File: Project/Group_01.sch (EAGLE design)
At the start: 1 part

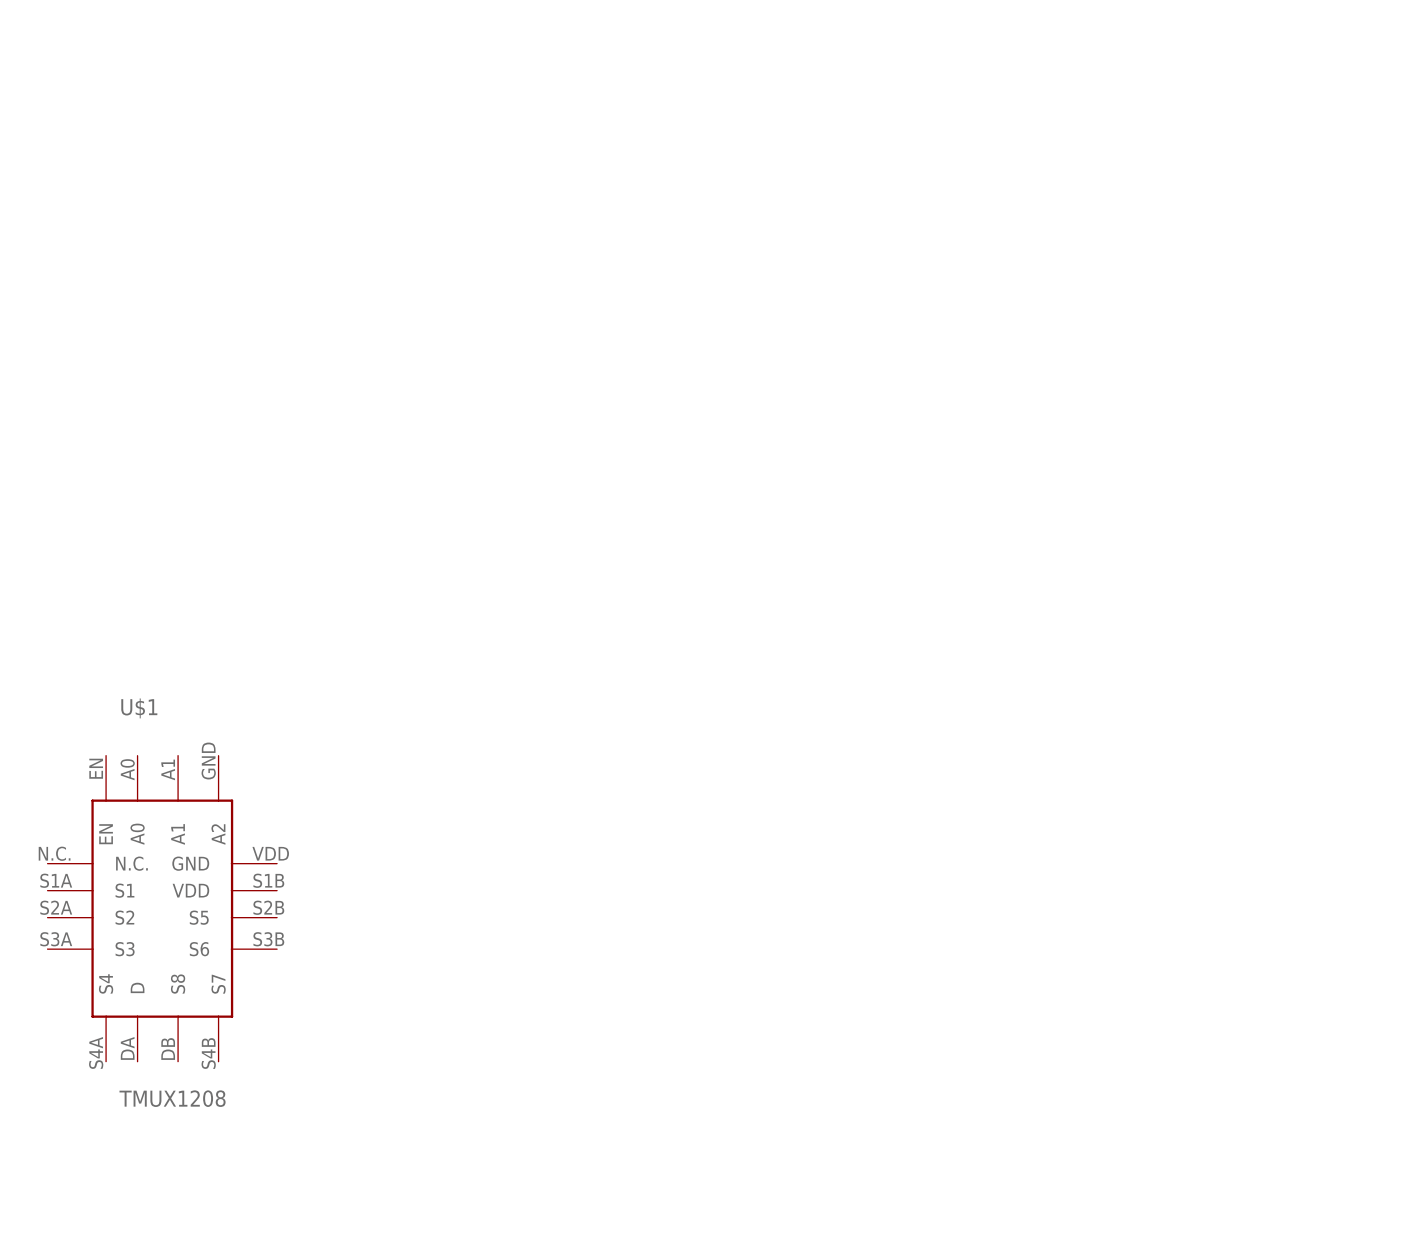
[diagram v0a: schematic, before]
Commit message: Added all components to schematics
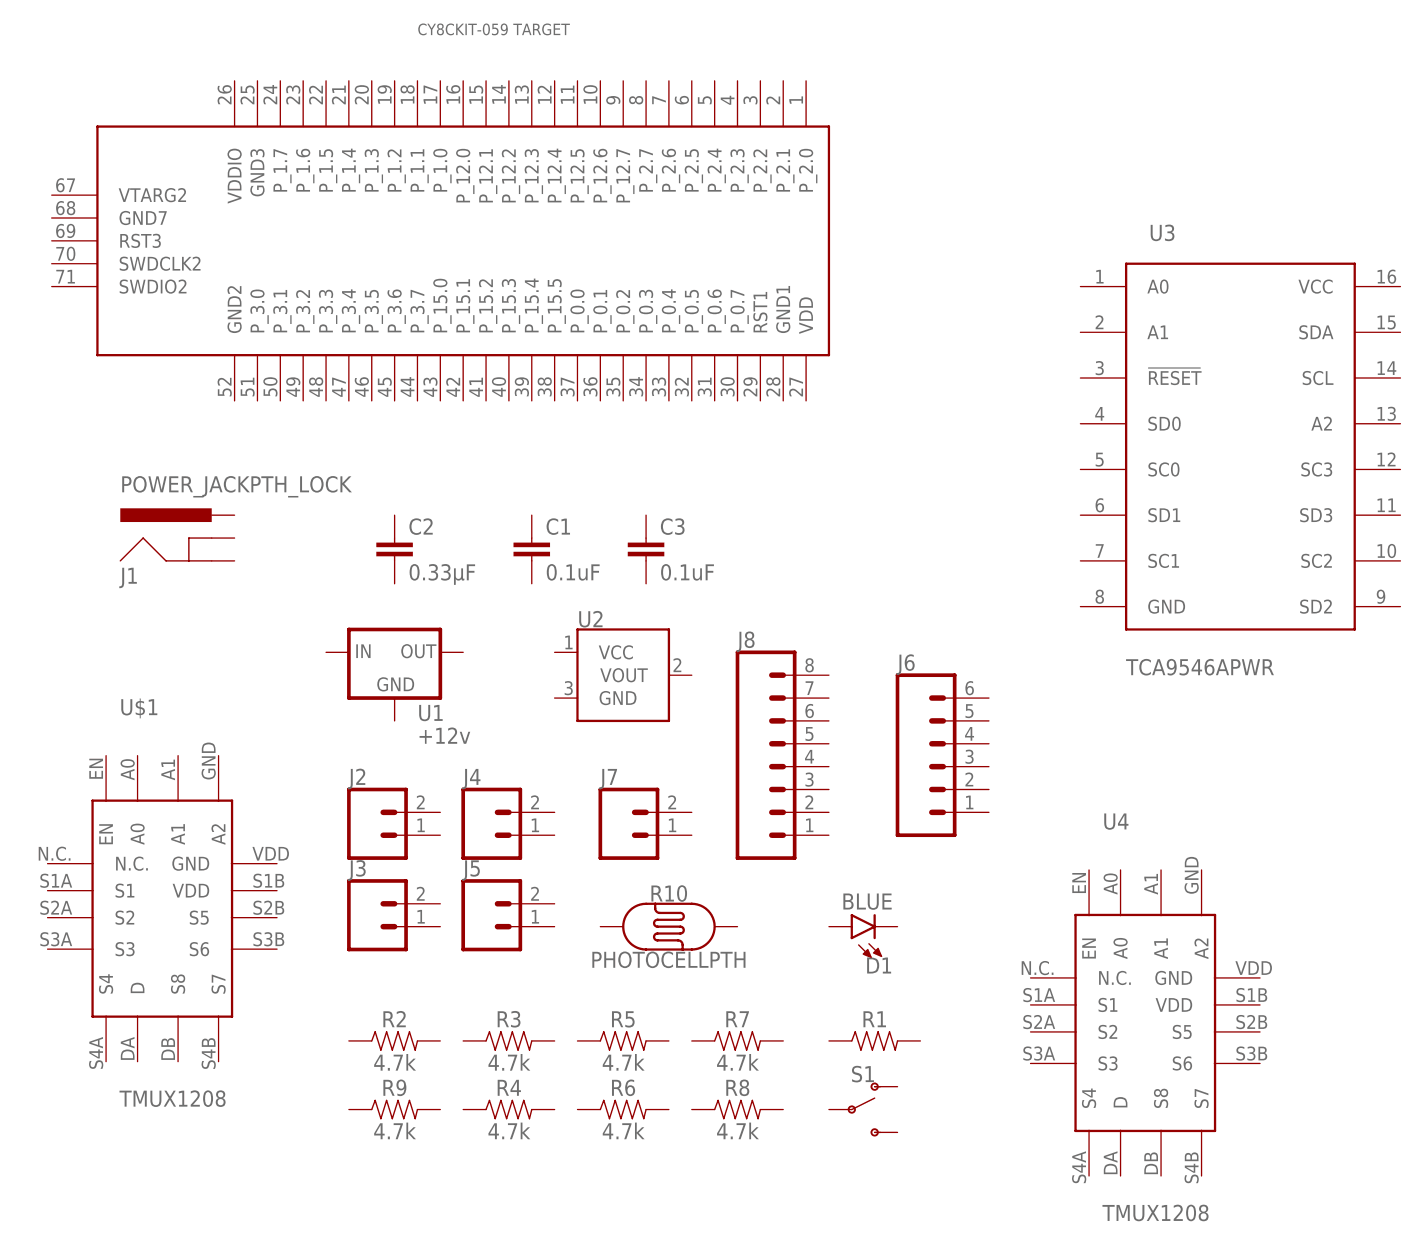
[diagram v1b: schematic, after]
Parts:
- added C1, C3: 0.1uF, SparkFun-Capacitors:0.1UF-KIT-EZ-50V-20%
- added C2: 0.33µF, SparkFun-Capacitors:0.33UF/330NF-0805-50V-10%
- added D1: BLUE, SparkFun-LED:LED-BLUE1206
- added J1: POWER_JACKPTH_LOCK, SparkFun-Connectors:POWER_JACKPTH_LOCK
- added J2, J3, J4, J5, J7: (no value), SparkFun-Connectors:CONN_02
- added J6: (no value), SparkFun-Connectors:CONN_06LOCK
- added J8: (no value), SparkFun-Connectors:CONN_08LOCK
- added R1: (no value), SparkFun-Resistors:RESISTORAXIAL-0.3
- added R10: PHOTOCELLPTH, SparkFun-Sensors:PHOTOCELLPTH
- added R2, R3, R4, R5, R6, R7, R8, R9: 4.7k, SparkFun-Resistors:4.7KOHM-0603-1/10W-1%
- added S1: (no value), SparkFun-Switches:SWITCH-SPDT-PTH-11.6X4.0MM
- added U$2: CY8CKIT-059_TARGET, CY8KIT-059:CY8CKIT-059_TARGET
- added U1: +12v, SparkFun-IC-Power:V_REG_78XX7812
- added U2: (no value), SparkFun-Sensors:TMP36GT9
- added U3: TCA9546APWR, Group_01_Library:TCA9546APWR
- added U4: TMUX1208, Group_01_Library:TMUX1208

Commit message: Schematics changes
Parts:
- added R11: 10k, SparkFun-Resistors:10KOHM-0603-1/10W-1%
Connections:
- new net 12V: C2.1, S1.O, U1.IN
- new net 5V: C1.1, J7.2, R10.P$2, U1.OUT, U2.VCC
- new net GND: C1.2, C2.2, J1.GND, J1.GNDBREAK, J7.1, R11.1, U1.GND, U2.GND
- new net N$1: J1.PWR, S1.P
- new net PHOTO_OUT: R10.P$1, R11.2
- new net TEMP_OUT: U2.VOUT
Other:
- moved on the sheet: C1, C2, C3, D1, J1, J6, J7, J8, R1, R10, S1, U1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

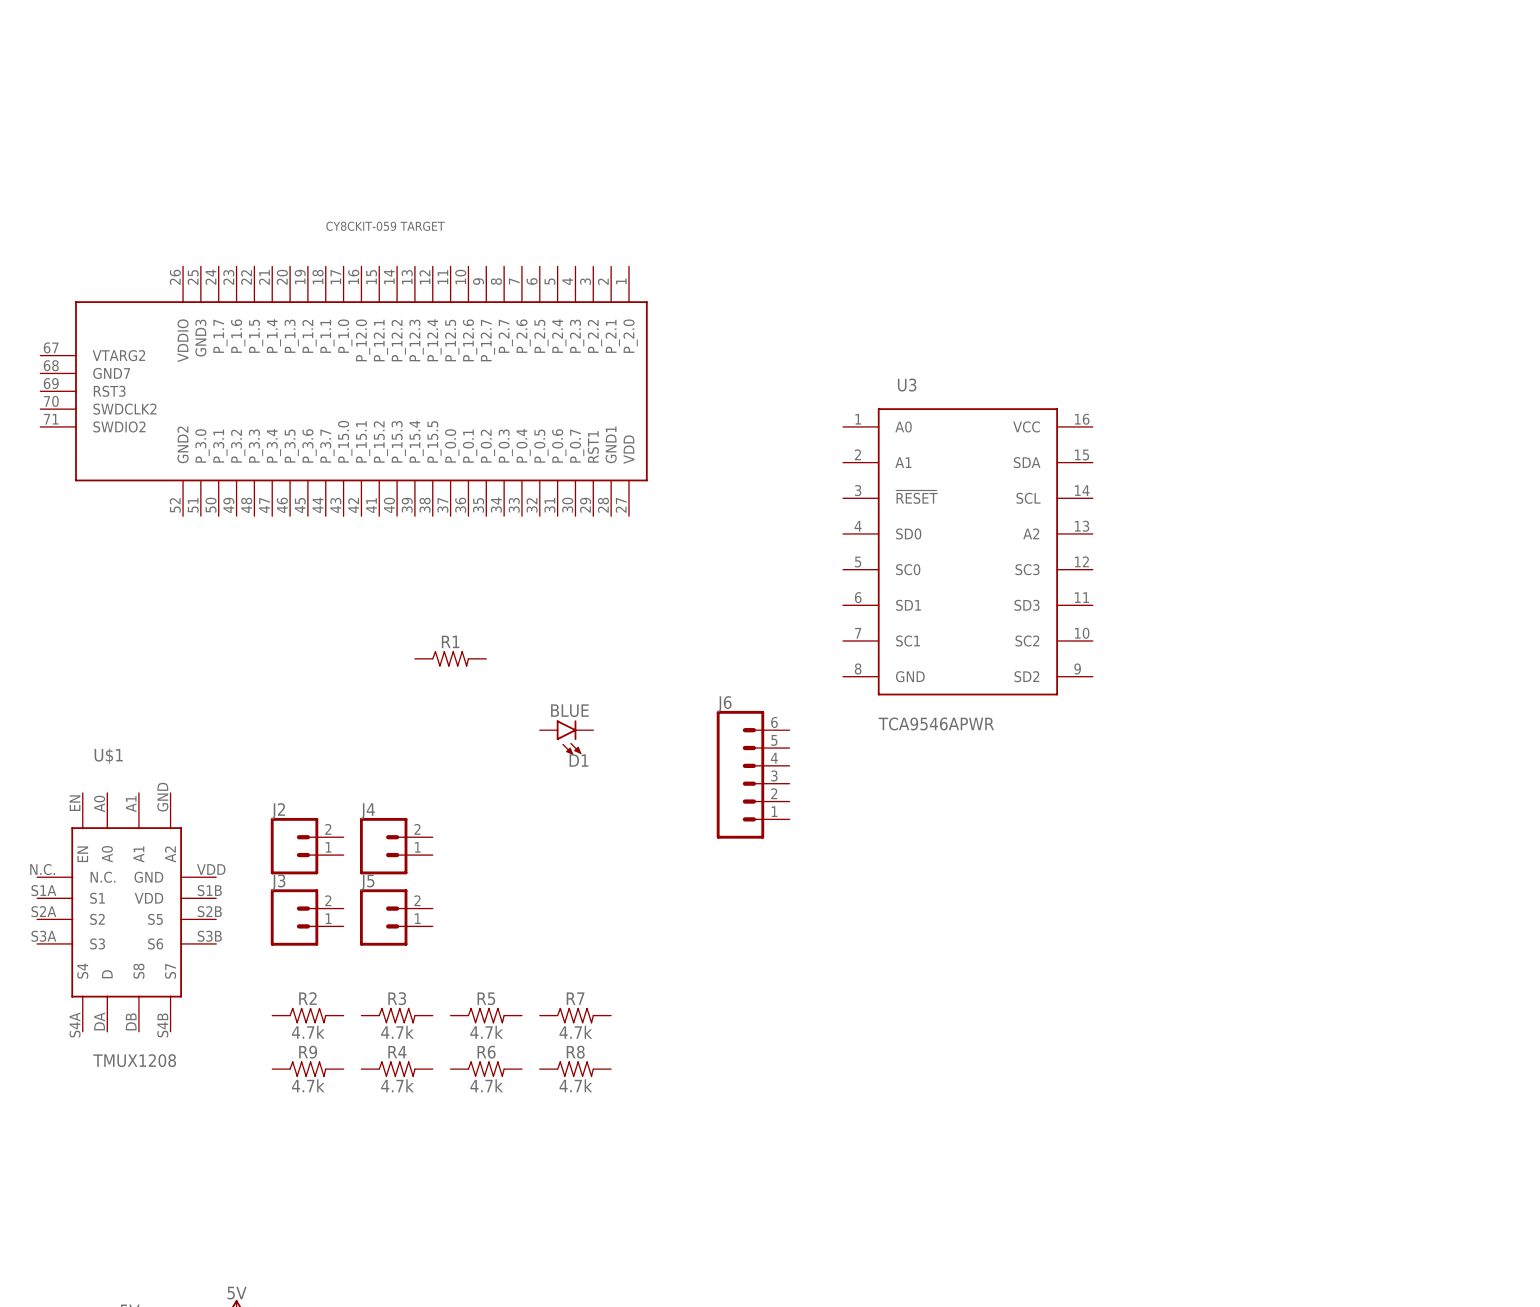
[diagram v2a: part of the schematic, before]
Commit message: Schematic update
Microcontroller, TCA and connectors all connected
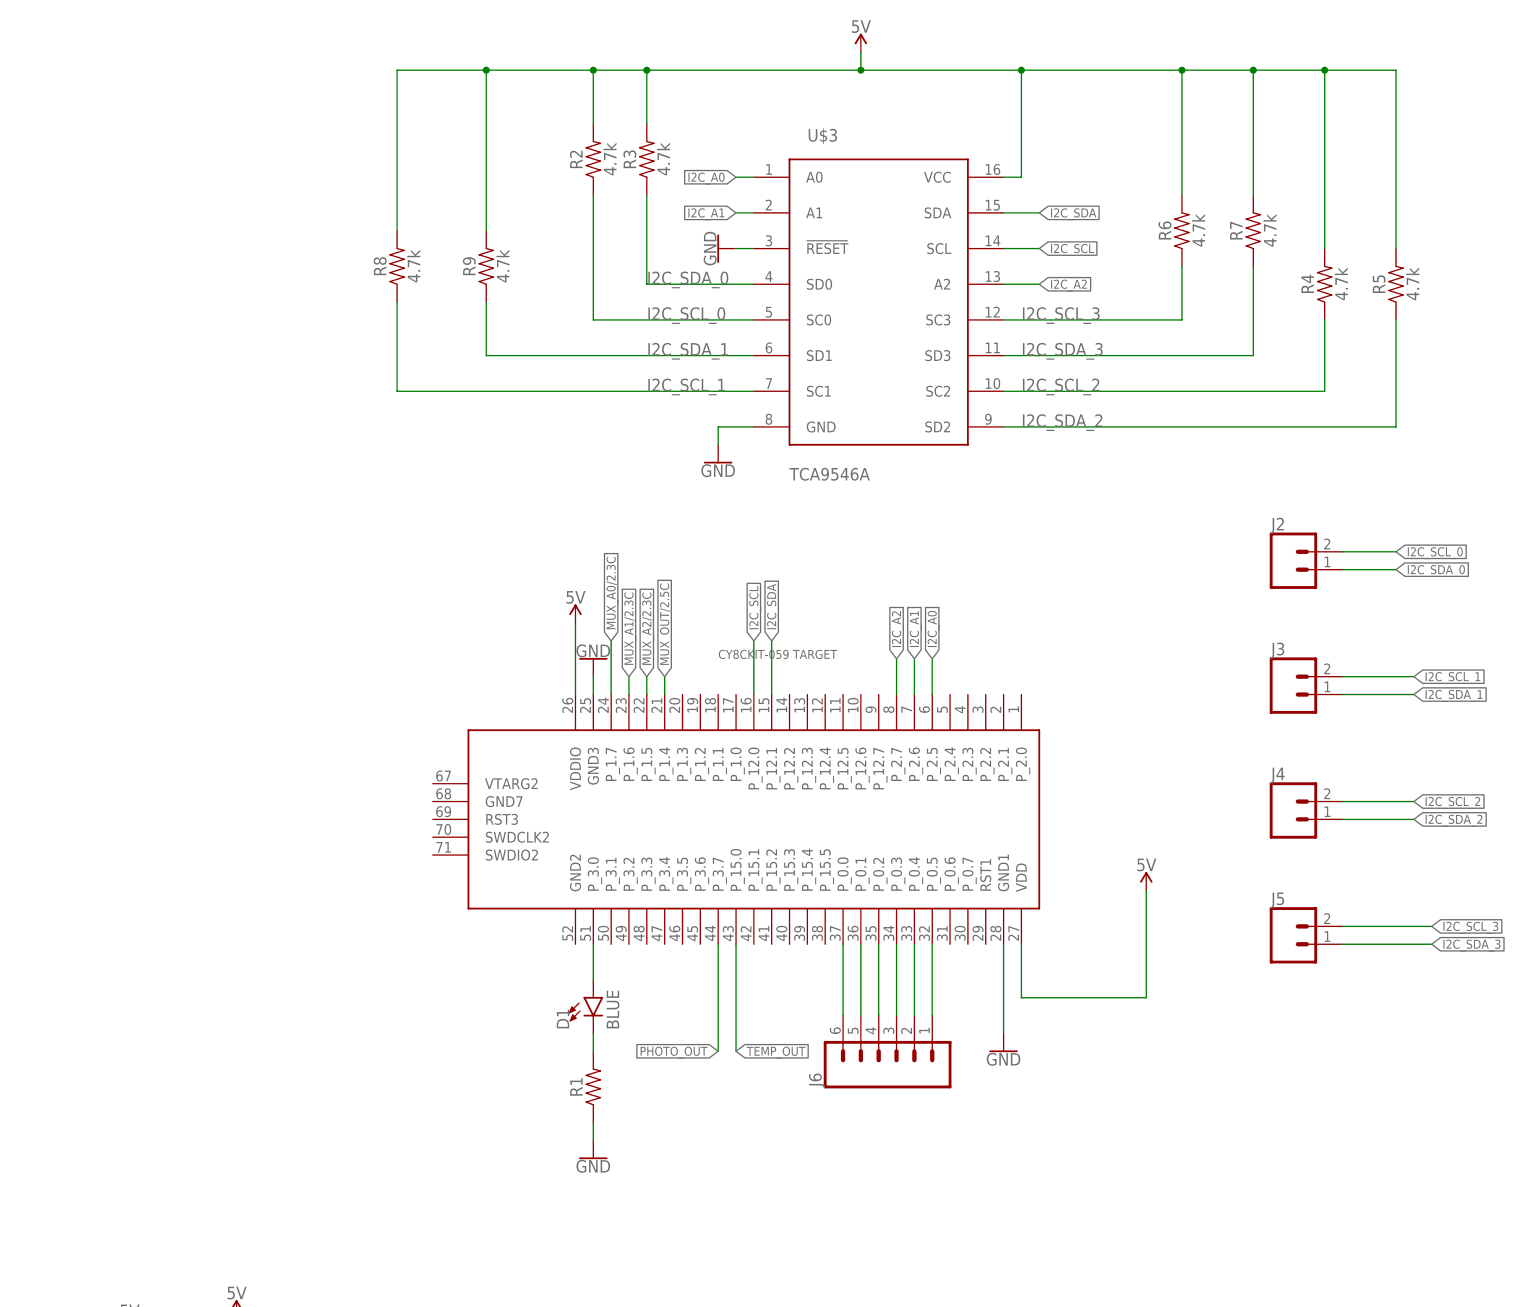
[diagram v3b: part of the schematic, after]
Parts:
- removed U$1: TMUX1208, Group_01_Library:TMUX1208
- removed U3: TCA9546APWR, Group_01_Library:TCA9546APWR
- added U$3: TCA9546A, Group_01_Library:TCA9546A
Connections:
- new net I2C_A0: U$2.P_2.5, U$3.A0
- new net I2C_A1: U$2.P_2.6, U$3.A1
- new net I2C_A2: U$2.P_2.7, U$3.A2
- new net I2C_SCL: U$2.P_12.0, U$3.SCL
- new net I2C_SCL_0: J2.2, R2.1, U$3.SC0
- new net I2C_SCL_1: J3.2, R8.1, U$3.SC1
- new net I2C_SCL_2: J4.2, R4.1, U$3.SC2
- new net I2C_SCL_3: J5.2, R6.1, U$3.SC3
- new net I2C_SDA: U$2.P_12.1, U$3.SDA
- new net I2C_SDA_0: J2.1, R3.1, U$3.SD0
- new net I2C_SDA_1: J3.1, R9.1, U$3.SD1
- new net I2C_SDA_2: J4.1, R5.1, U$3.SD2
- new net I2C_SDA_3: J5.1, R7.1, U$3.SD3
- new net MUX_A0/2.3C: U$2.P_1.7
- new net MUX_A1/2.3C: U$2.P_1.6
- new net MUX_A2/2.3C: U$2.P_1.5
- new net MUX_OUT/2.5C: U$2.P_1.4
- new net N$2: J6.1, U$2.P_0.5
- new net N$3: J6.2, U$2.P_0.4
- new net N$4: J6.3, U$2.P_0.3
- new net N$5: J6.4, U$2.P_0.2
- new net N$6: J6.5, U$2.P_0.1
- new net N$7: J6.6, U$2.P_0.0
- new net N$8: D1.A, U$2.P_3.0
- new net N$9: D1.C, R1.2
- net 5V: now also R2.2, R3.2, R4.2, R5.2, R6.2, R7.2, R8.2, R9.2, U$2.VDD, U$2.VDDIO, U$3.VCC
- net GND: now also R1.1, U$2.GND1, U$2.GND3, U$3.!RESET!, U$3.GND
- net PHOTO_OUT: now also U$2.P_3.7
- net TEMP_OUT: now also U$2.P_15.0
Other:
- moved on the sheet: D1, J2, J3, J4, J5, J6, R1, R2, R3, R4, R5, R6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
